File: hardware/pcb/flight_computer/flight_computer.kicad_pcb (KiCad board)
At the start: 4 copper layers, 64 x 64 mm, 95 parts, among them J1 NRF24L01, J2 BATT_TERMINAL, J3 5V Terminal, J4 Pyro 1, J5 Pyro 2, J6 Servo, J7 Servo, J8 Conn_01x02, J9 Aux Ports, Q1 AO3401A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

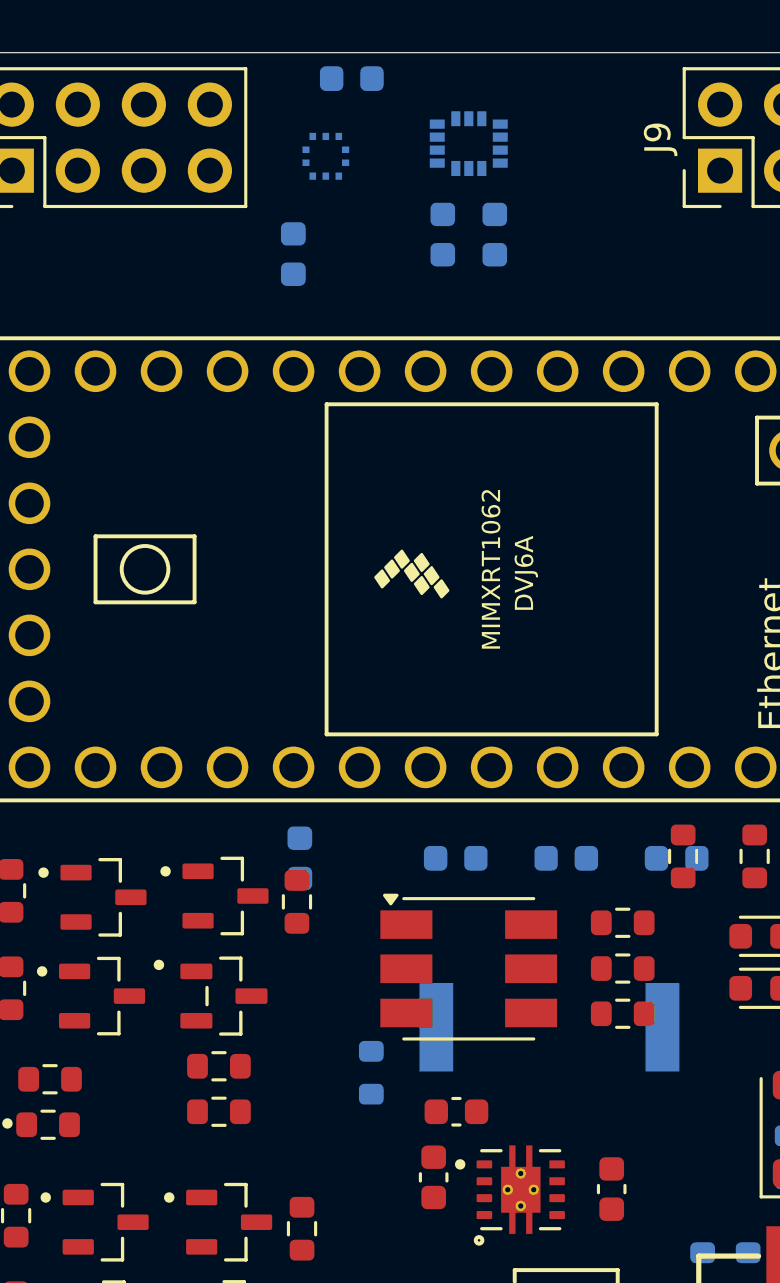
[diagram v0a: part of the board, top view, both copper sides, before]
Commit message: Added 3D model
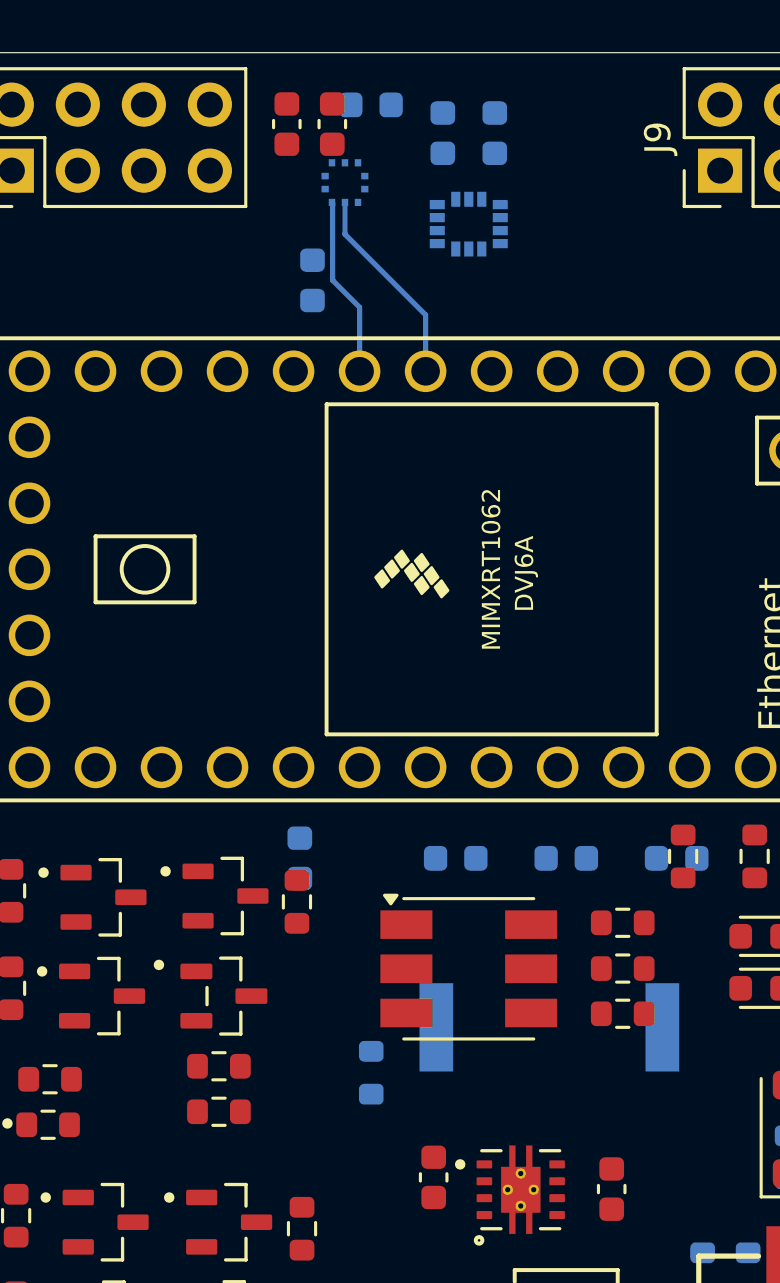
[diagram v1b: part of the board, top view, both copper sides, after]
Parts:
- removed C8: 10 uF, Capacitor_SMD:C_0603_1608Metric
- added C16: 0.1 uF, Capacitor_SMD:C_0603_1608Metric, F.Cu at (143.0, 58.2)
- added C17: 10 uF, Capacitor_SMD:C_0603_1608Metric, F.Cu at (144.8, 58.2)
- moved C13 4.38 mm to (151.0, 58.6), turned to 90 degrees
- moved C15 4.38 mm to (149.0, 58.6), turned to 90 degrees
- moved U5 3.10 mm to (150.0, 62.1), turned to 0 degrees
- moved C14 1.25 mm to (146.2, 57.5)
- moved C4 1.25 mm to (144.0, 64.3)
- moved U4 1.25 mm to (145.2, 60.5), turned to 180 degrees
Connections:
- Q2 pad 3: /Pyro 1/+8.4V -> /Power/VIN
- Q6 pad 3: /Pyro 2/+8.4V -> /Power/VIN
- R23 pad 1: /Pyro 2/+8.4V -> /Power/VIN
- R8 pad 1: /Pyro 1/+8.4V -> /Power/VIN
- U6 pad 25: /MCU/LED_B -> /Indication/B
- U6 pad 36: /MCU/LED_R -> /Indication/R
- U6 pad 37: /MCU/LED_G -> /Indication/G
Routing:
- net /Barometer/SDI: track 0.00 -> 7.78 mm
- net /Barometer/SDO: track 0.00 -> 6.94 mm
